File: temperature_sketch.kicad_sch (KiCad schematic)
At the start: 1 part, among them U2 MCP9808_DFN

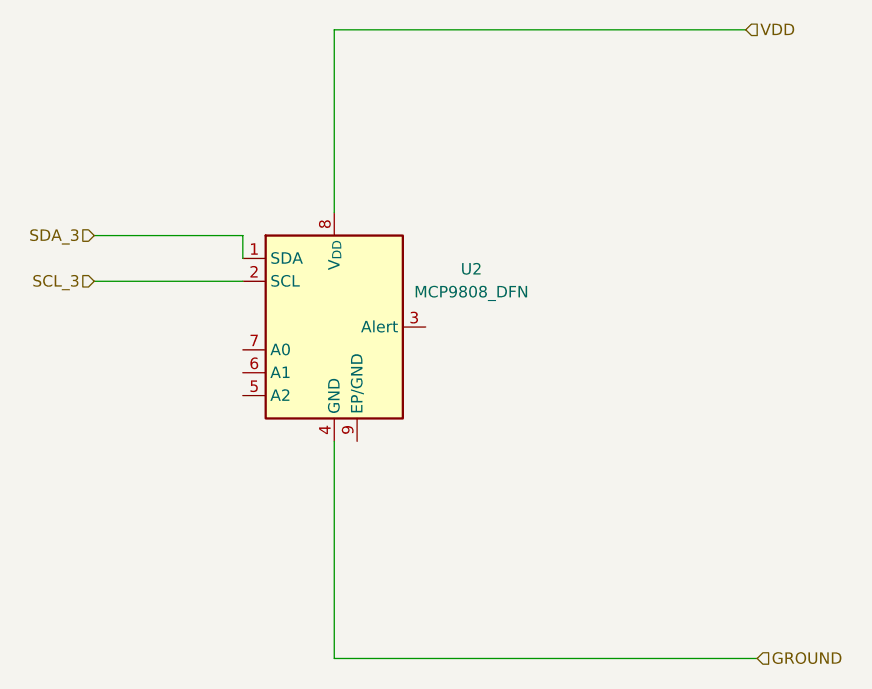
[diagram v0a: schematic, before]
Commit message: Corrected footprint assignment errors
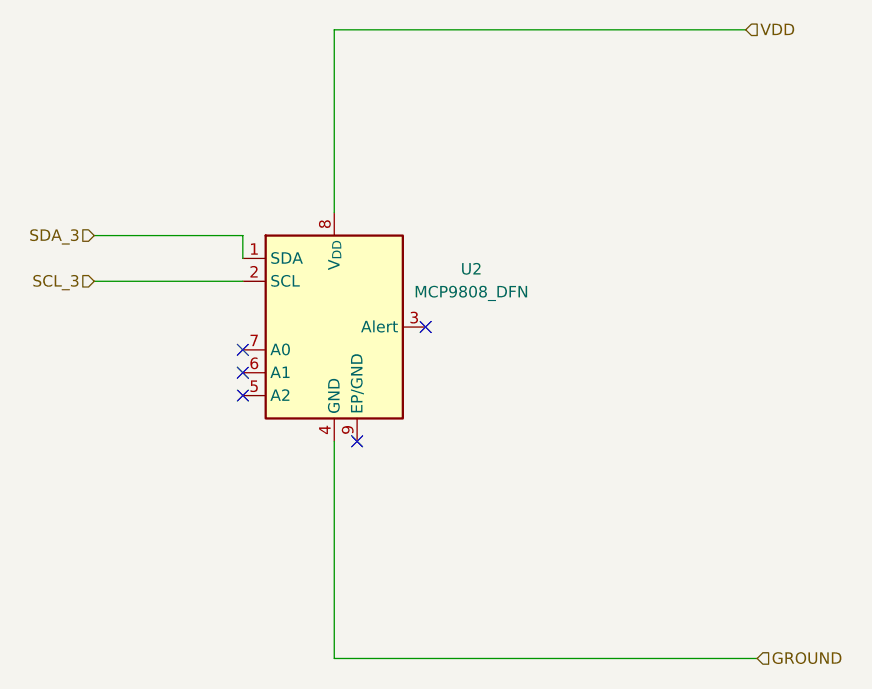
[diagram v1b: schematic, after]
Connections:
- no-connect marks 0 -> 5
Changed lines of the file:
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@@
 	(generator_version "9.0")
 	(paper "A4")
+	(no_connect
+		(at 114.3 86.36)
+	)
+	(no_connect
+		(at 127 93.98)
+	)
+	(no_connect
+		(at 134.62 81.28)
+	)
+	(no_connect
+		(at 114.3 83.82)
+	)
+	(no_connect
+		(at 114.3 88.9)
+	)
 	(wire
 		(pts
